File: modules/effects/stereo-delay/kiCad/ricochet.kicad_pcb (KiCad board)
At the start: 2 copper layers, 81 x 111 mm, 37 parts, among them J1 INPUT, J2 OUTPUT, J3 PWR, U1 TL074

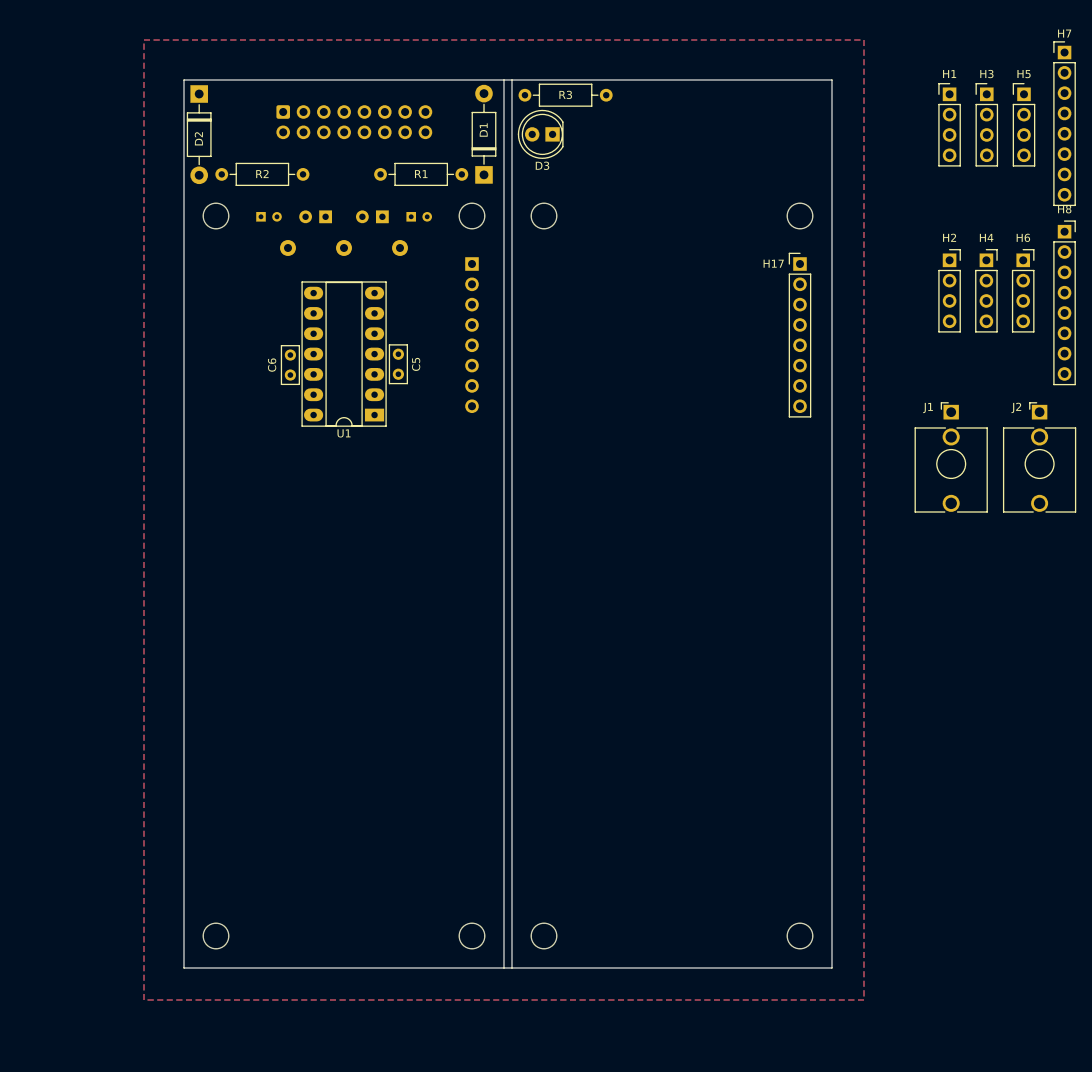
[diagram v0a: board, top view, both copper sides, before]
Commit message: Midi 2 CV (Midas) Rework; Delay (Richochet) Rework. Programming, backups for WeAct CV
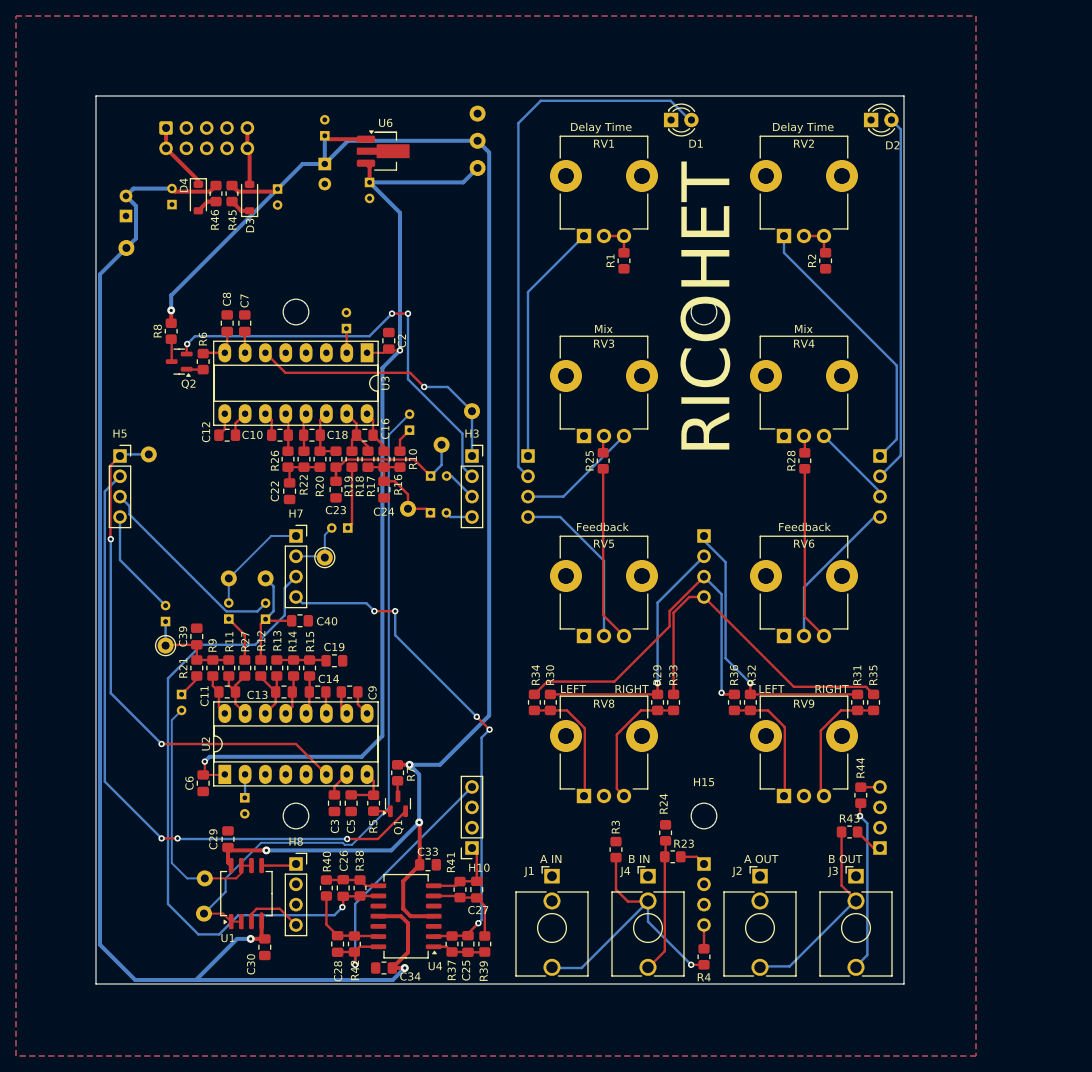
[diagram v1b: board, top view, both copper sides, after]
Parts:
- removed H16: MountingHole, MountingHole:MountingHole_3.2mm_M3
- removed H17: H17, Synth:PinHeader_1x08_P2.54mm_Vertical
- removed H18: H18, Synth:PinSocket_1x08_P2.54mm_Vertical
- added C10: 100nF, Capacitor_SMD:C_0805_2012Metric_Pad1.18x1.45mm_HandSolder, F.Cu at (73.0, 92.4)
- added C11: 560pF, Capacitor_SMD:C_0805_2012Metric_Pad1.18x1.45mm_HandSolder, F.Cu at (66.4, 124.5)
- added C12: 100nF, Capacitor_SMD:C_0805_2012Metric_Pad1.18x1.45mm_HandSolder, F.Cu at (66.4, 92.4)
- added C13: 560pF, Capacitor_SMD:C_0805_2012Metric_Pad1.18x1.45mm_HandSolder, F.Cu at (73.5, 124.5)
- added C14: 100nF, Capacitor_SMD:C_0805_2012Metric_Pad1.18x1.45mm_HandSolder, F.Cu at (77.7, 124.5)
- added C15: 4.7uF, Capacitor_THT:CP_Radial_D4.0mm_P2.00mm, B.Cu at (89.2, 91.8)
- added C16: 560pF, Capacitor_SMD:C_0805_2012Metric_Pad1.18x1.45mm_HandSolder, F.Cu at (83.6, 92.4)
- added C17: 4.7uF, Capacitor_THT:CP_Radial_D4.0mm_P2.00mm, B.Cu at (60.7, 124.8)
- added C18: 560pF, Capacitor_SMD:C_0805_2012Metric_Pad1.18x1.45mm_HandSolder, F.Cu at (77.0, 92.4)
- added C19: 3.3nF, Capacitor_SMD:C_0805_2012Metric_Pad1.18x1.45mm_HandSolder, F.Cu at (79.8, 120.6)
- added C20: 4.7uF, Capacitor_THT:CP_Radial_D4.0mm_P2.00mm, B.Cu at (58.7, 115.7)
- added C21: 10uF, Capacitor_THT:CP_Radial_D4.0mm_P2.00mm, B.Cu at (71.2, 115.4)
- added C22: 3.3nF, Capacitor_SMD:C_0805_2012Metric_Pad1.18x1.45mm_HandSolder, F.Cu at (74.2, 99.4)
- added C23: 10nF, Capacitor_SMD:C_0805_2012Metric_Pad1.18x1.45mm_HandSolder, F.Cu at (80.0, 99.2)
- added C24: 3.9nF, Capacitor_SMD:C_0805_2012Metric_Pad1.18x1.45mm_HandSolder, F.Cu at (86.0, 99.2)
- added C25: 27pF, Capacitor_SMD:C_0805_2012Metric_Pad1.18x1.45mm_HandSolder, F.Cu at (96.5, 156.0)
- added C26: 27pF, Capacitor_SMD:C_0805_2012Metric_Pad1.18x1.45mm_HandSolder, F.Cu at (80.9, 149.0)
- added C27: 47pF, Capacitor_SMD:C_0805_2012Metric_Pad1.18x1.45mm_HandSolder, F.Cu at (97.6, 149.2)
- added C28: 47pF, Capacitor_SMD:C_0805_2012Metric_Pad1.18x1.45mm_HandSolder, F.Cu at (80.2, 156.0)
- added C29: 0.1uF, Capacitor_SMD:C_0805_2012Metric_Pad1.18x1.45mm_HandSolder, F.Cu at (66.5, 142.9)
- added C30: 0.1uF, Capacitor_SMD:C_0805_2012Metric_Pad1.18x1.45mm_HandSolder, F.Cu at (71.1, 156.4)
- added C31: 47uF, Capacitor_THT:CP_Radial_D6.3mm_P2.50mm, B.Cu at (78.6, 58.5)
- added C32: 47uF, Capacitor_THT:CP_Radial_D6.3mm_P2.50mm, B.Cu at (53.8, 65.0)
- added C33: 0.1uF, Capacitor_SMD:C_0805_2012Metric_Pad1.18x1.45mm_HandSolder, F.Cu at (91.5, 146.1)
- added C34: 0.1uF, Capacitor_SMD:C_0805_2012Metric_Pad1.18x1.45mm_HandSolder, F.Cu at (86.0, 159.0)
- added C35: 0.1uF, Capacitor_THT:CP_Radial_D4.0mm_P2.00mm, B.Cu at (78.6, 55.0)
- added C36: 0.1uF, Capacitor_THT:CP_Radial_D4.0mm_P2.00mm, B.Cu at (59.5, 63.6)
- added C37: 0.1uF, Capacitor_THT:CP_Radial_D4.0mm_P2.00mm, B.Cu at (72.7, 61.6)
- added C38: 0.1uF, Capacitor_THT:CP_Radial_D4.0mm_P2.00mm, B.Cu at (84.2, 60.8)
- added C39: 3.9nF, Capacitor_SMD:C_0805_2012Metric_Pad1.18x1.45mm_HandSolder, F.Cu at (62.6, 117.6)
- added C40: 10nF, Capacitor_SMD:C_0805_2012Metric_Pad1.18x1.45mm_HandSolder, F.Cu at (75.5, 115.6)
- added C41: 10uF, Capacitor_THT:CP_Radial_D4.0mm_P2.00mm, B.Cu at (66.6, 115.4)
- added C42: 10uF, Capacitor_THT:CP_Radial_D4.0mm_P2.00mm, B.Cu at (81.5, 104.0)
- added C43: 10uF, Capacitor_THT:CP_Radial_D4.0mm_P2.00mm, B.Cu at (91.8, 97.5)
- added C44: 4.7uF, Capacitor_THT:CP_Radial_D4.0mm_P2.00mm, B.Cu at (91.8, 102.1)
- added C7: 100nF, Capacitor_SMD:C_0805_2012Metric_Pad1.18x1.45mm_HandSolder, F.Cu at (68.6, 78.4)
- added C8: 100nF, Capacitor_SMD:C_0805_2012Metric_Pad1.18x1.45mm_HandSolder, F.Cu at (66.4, 78.4)
- added C9: 100nF, Capacitor_SMD:C_0805_2012Metric_Pad1.18x1.45mm_HandSolder, F.Cu at (81.7, 124.5)
- added D4: 1N5819, Diode_SMD:D_SOD-123, F.Cu at (62.8, 62.7)
- added J4: INPUT, Synth:Jack_3.5mm_QingPu_WQP-PJ398SM_Vertical_CircularHoles, F.Cu at (119.0, 154.0)
- added Q1: 2N3904, Package_TO_SOT_SMD:SOT-23, F.Cu at (87.8, 138.5)
- added Q2: 2N3904, Package_TO_SOT_SMD:SOT-23, F.Cu at (60.4, 83.2)
- added R10: 15K, Resistor_SMD:R_0805_2012Metric_Pad1.20x1.40mm_HandSolder, F.Cu at (88.0, 95.4)
- added R11: 10K, Resistor_SMD:R_0805_2012Metric_Pad1.20x1.40mm_HandSolder, F.Cu at (66.6, 121.5)
- added R12: 5.6K, Resistor_SMD:R_0805_2012Metric_Pad1.20x1.40mm_HandSolder, F.Cu at (70.6, 121.5)
- added R13: 15K, Resistor_SMD:R_0805_2012Metric_Pad1.20x1.40mm_HandSolder, F.Cu at (72.6, 121.5)
- added R14: 10K, Resistor_SMD:R_0805_2012Metric_Pad1.20x1.40mm_HandSolder, F.Cu at (74.7, 121.5)
- added R15: 10K, Resistor_SMD:R_0805_2012Metric_Pad1.20x1.40mm_HandSolder, F.Cu at (76.7, 121.5)
- added R16: 10K, Resistor_SMD:R_0805_2012Metric_Pad1.20x1.40mm_HandSolder, F.Cu at (86.0, 95.4)
- added R17: 10K, Resistor_SMD:R_0805_2012Metric_Pad1.20x1.40mm_HandSolder, F.Cu at (84.0, 95.4)
- added R18: 4.7K, Resistor_SMD:R_0805_2012Metric_Pad1.20x1.40mm_HandSolder, F.Cu at (82.0, 95.4)
- added R19: 5.6K, Resistor_SMD:R_0805_2012Metric_Pad1.20x1.40mm_HandSolder, F.Cu at (80.0, 95.4)
- added R20: 15K, Resistor_SMD:R_0805_2012Metric_Pad1.20x1.40mm_HandSolder, F.Cu at (78.0, 95.4)
- added R21: 15K, Resistor_SMD:R_0805_2012Metric_Pad1.20x1.40mm_HandSolder, F.Cu at (62.6, 121.5)
- added R22: 10K, Resistor_SMD:R_0805_2012Metric_Pad1.20x1.40mm_HandSolder, F.Cu at (76.0, 95.4)
- added R23: 1K, Resistor_SMD:R_0805_2012Metric_Pad1.20x1.40mm_HandSolder, F.Cu at (122.1, 145.1)
- added R24: 100K, Resistor_SMD:R_0805_2012Metric_Pad1.20x1.40mm_HandSolder, F.Cu at (121.2, 142.1)
- added R25: 10K, Resistor_SMD:R_0805_2012Metric_Pad1.20x1.40mm_HandSolder, F.Cu at (113.4, 95.6)
- added R26: 10K, Resistor_SMD:R_0805_2012Metric_Pad1.20x1.40mm_HandSolder, F.Cu at (74.0, 95.4)
- added R27: 4.7K, Resistor_SMD:R_0805_2012Metric_Pad1.20x1.40mm_HandSolder, F.Cu at (68.6, 121.5)
- added R28: 10K, Resistor_SMD:R_0805_2012Metric_Pad1.20x1.40mm_HandSolder, F.Cu at (138.6, 95.6)
- added R29: 10K, Resistor_SMD:R_0805_2012Metric_Pad1.20x1.40mm_HandSolder, F.Cu at (120.2, 125.8)
- added R30: 10K, Resistor_SMD:R_0805_2012Metric_Pad1.20x1.40mm_HandSolder, F.Cu at (106.8, 125.8)
- added R31: 10K, Resistor_SMD:R_0805_2012Metric_Pad1.20x1.40mm_HandSolder, F.Cu at (145.2, 125.8)
- added R32: 10K, Resistor_SMD:R_0805_2012Metric_Pad1.20x1.40mm_HandSolder, F.Cu at (131.8, 125.8)
- added R33: 10K, Resistor_SMD:R_0805_2012Metric_Pad1.20x1.40mm_HandSolder, F.Cu at (122.2, 125.8)
- added R34: 10K, Resistor_SMD:R_0805_2012Metric_Pad1.20x1.40mm_HandSolder, F.Cu at (104.8, 125.8)
- added R35: 10K, Resistor_SMD:R_0805_2012Metric_Pad1.20x1.40mm_HandSolder, F.Cu at (147.2, 125.8)
- added R36: 10K, Resistor_SMD:R_0805_2012Metric_Pad1.20x1.40mm_HandSolder, F.Cu at (129.8, 125.8)
- added R37: 33K, Resistor_SMD:R_0805_2012Metric_Pad1.20x1.40mm_HandSolder, F.Cu at (94.5, 156.0)
- added R38: 33K, Resistor_SMD:R_0805_2012Metric_Pad1.20x1.40mm_HandSolder, F.Cu at (83.0, 149.0)
- added R39: 10K, Resistor_SMD:R_0805_2012Metric_Pad1.20x1.40mm_HandSolder, F.Cu at (98.6, 156.0)
- added R4: 1K, Resistor_SMD:R_0805_2012Metric_Pad1.20x1.40mm_HandSolder, F.Cu at (126.0, 157.6)
- added R40: 10K, Resistor_SMD:R_0805_2012Metric_Pad1.20x1.40mm_HandSolder, F.Cu at (78.8, 149.0)
- added R41: 10K, Resistor_SMD:R_0805_2012Metric_Pad1.20x1.40mm_HandSolder, F.Cu at (95.5, 149.2)
- added R42: 10K, Resistor_SMD:R_0805_2012Metric_Pad1.20x1.40mm_HandSolder, F.Cu at (82.3, 156.0)
- added R43: 1K, Resistor_SMD:R_0805_2012Metric_Pad1.20x1.40mm_HandSolder, F.Cu at (144.2, 142.0)
- added R44: 1K, Resistor_SMD:R_0805_2012Metric_Pad1.20x1.40mm_HandSolder, F.Cu at (145.6, 137.4)
- added R45: 10R, Resistor_SMD:R_0805_2012Metric_Pad1.20x1.40mm_HandSolder, F.Cu at (67.0, 62.2)
- added R46: 10R, Resistor_SMD:R_0805_2012Metric_Pad1.20x1.40mm_HandSolder, F.Cu at (65.0, 62.2)
- added R5: 1K, Resistor_SMD:R_0805_2012Metric_Pad1.20x1.40mm_HandSolder, F.Cu at (84.7, 138.4)
- added R6: 1K, Resistor_SMD:R_0805_2012Metric_Pad1.20x1.40mm_HandSolder, F.Cu at (63.4, 83.2)
- added R7: 100K, Resistor_SMD:R_0805_2012Metric_Pad1.20x1.40mm_HandSolder, F.Cu at (87.7, 134.6)
- added R8: 100K, Resistor_SMD:R_0805_2012Metric_Pad1.20x1.40mm_HandSolder, F.Cu at (59.4, 79.4)
- added R9: 10K, Resistor_SMD:R_0805_2012Metric_Pad1.20x1.40mm_HandSolder, F.Cu at (64.6, 121.5)
- added RV1: B50K, Synth:Potentiometer_TT_P0915N, F.Cu at (113.5, 60.0)
- added RV2: B50K, Synth:Potentiometer_TT_P0915N, F.Cu at (138.5, 60.0)
- added RV3: B100K, Synth:Potentiometer_TT_P0915N, F.Cu at (113.5, 85.0)
- added RV4: B100K, Synth:Potentiometer_TT_P0915N, F.Cu at (138.5, 85.0)
- added RV5: B100K, Synth:Potentiometer_TT_P0915N, F.Cu at (113.5, 110.0)
- added RV6: B100K, Synth:Potentiometer_TT_P0915N, F.Cu at (138.5, 110.0)
- added RV8: B25K, Synth:Potentiometer_TT_P0915N, F.Cu at (113.5, 130.0)
- added RV9: B25K, Synth:Potentiometer_TT_P0915N, F.Cu at (138.5, 130.0)
- added TP10: POST_FEEDBACK_CH_2, Connector_Pin:Pin_D1.0mm_L10.0mm, F.Cu at (58.7, 118.7)
- added TP11: POST_FEEDBACK_CH_1, Connector_Pin:Pin_D1.0mm_L10.0mm, B.Cu at (89.0, 101.6)
- added TP12: MIX_INPUT_CH_2, Connector_Pin:Pin_D1.0mm_L10.0mm, B.Cu at (71.2, 110.3)
- added TP13: MIX_INPUT_CH_1, Connector_Pin:Pin_D1.0mm_L10.0mm, B.Cu at (93.2, 93.6)
- added TP14: +5V, Connector_Pin:Pin_D1.0mm_L10.0mm, B.Cu at (97.7, 59.0)
- added TP4: INPUT_CH_1, Connector_Pin:Pin_D1.0mm_L10.0mm, B.Cu at (63.5, 152.2)
- added TP5: INPUT_CH_2, Connector_Pin:Pin_D1.0mm_L10.0mm, B.Cu at (63.6, 147.8)
- added TP6: OUTPUT_CH_1, Connector_Pin:Pin_D1.0mm_L10.0mm, F.Cu at (78.6, 107.7)
- added TP7: OUTPUT_CH_2, Connector_Pin:Pin_D1.0mm_L10.0mm, B.Cu at (66.6, 110.3)
- added TP8: DELAY_TIME_CH_2, Connector_Pin:Pin_D1.0mm_L10.0mm, B.Cu at (56.6, 94.8)
- added TP9: DELAY_TIME_CH_1, Connector_Pin:Pin_D1.0mm_L10.0mm, B.Cu at (97.0, 89.4)
- added U2: PT2399, Package_DIP:DIP-16_W7.62mm_Socket_LongPads, F.Cu at (66.1, 134.8)
- added U3: PT2399, Package_DIP:DIP-16_W7.62mm_Socket_LongPads, F.Cu at (83.9, 82.1)
- added U4: TL074, Package_SO:SO-14_5.3x10.2mm_P1.27mm, F.Cu at (88.8, 152.5)
- added U6: L7805, Package_TO_SOT_SMD:SOT-89-3_Handsoldering, F.Cu at (86.2, 56.9)
- C1: value 47uF -> 10uF; footprint Capacitor_THT:CP_Radial_D6.3mm_P2.50mm -> Capacitor_THT:CP_Radial_D4.0mm_P2.00mm
- C2: value 47uF -> 100nF; footprint Capacitor_THT:CP_Radial_D6.3mm_P2.50mm -> Capacitor_SMD:C_0805_2012Metric_Pad1.18x1.45mm_HandSolder; moved to F.Cu
- C3: value 0.1uF -> 100nF; footprint Capacitor_THT:CP_Radial_D4.0mm_P2.00mm -> Capacitor_SMD:C_0805_2012Metric_Pad1.18x1.45mm_HandSolder; moved to F.Cu
- C4: value 0.1uF -> 10uF
- C5, C6: value 0.1uF -> 100nF; footprint Capacitor_THT:C_Rect_L4.6mm_W2.0mm_P2.50mm_MKS02_FKP02 -> Capacitor_SMD:C_0805_2012Metric_Pad1.18x1.45mm_HandSolder
- D1, D2: value 1N5819 -> LED; footprint Synth:D_DO-41_SOD81_P10.16mm_Horizontal -> Synth:LED_D3.0mm
- D3: value LED -> 1N5819; footprint Synth:LED_D5.0mm (center Aligned) -> Diode_SMD:D_SOD-123
- H1: value H1 -> Conn_02x05_PWR_Eurorack; footprint Synth:PinHeader_1x04_P2.54mm_Vertical -> Synth:IDC-Header_2x05_P2.54mm_Vertical; moved to B.Cu
- H10: value MountingHole -> PinSocket_01x04; footprint MountingHole:MountingHole_3.2mm_M3 -> Synth:PinSocket_1x04_P2.54mm_Vertical
- H11, H9: value MountingHole -> PinHeader_01x04; footprint MountingHole:MountingHole_3.2mm_M3 -> Synth:PinHeader_1x04_P2.54mm_Vertical; moved to B.Cu
- H2: value H3 -> PinHeader_01x04; footprint Synth:PinSocket_1x04_P2.54mm_Vertical -> Synth:PinHeader_1x04_P2.54mm_Vertical; moved to B.Cu
- H3: value H5 -> PinSocket_01x04; footprint Synth:PinHeader_1x04_P2.54mm_Vertical -> Synth:PinSocket_1x04_P2.54mm_Vertical
- H4: value H6 -> PinHeader_01x04; footprint Synth:PinSocket_1x04_P2.54mm_Vertical -> Synth:PinHeader_1x04_P2.54mm_Vertical; moved to B.Cu
- H5: value H7 -> PinSocket_01x04; footprint Synth:PinHeader_1x04_P2.54mm_Vertical -> Synth:PinSocket_1x04_P2.54mm_Vertical
- H6: value H8 -> PinHeader_01x04; footprint Synth:PinSocket_1x04_P2.54mm_Vertical -> Synth:PinHeader_1x04_P2.54mm_Vertical; moved to B.Cu
- H7: value H2 -> PinSocket_01x04; footprint Synth:PinHeader_1x08_P2.54mm_Vertical -> Synth:PinSocket_1x04_P2.54mm_Vertical
- H8: value H4 -> PinSocket_01x04; footprint Synth:PinSocket_1x08_P2.54mm_Vertical -> Synth:PinSocket_1x04_P2.54mm_Vertical
- J2: value OUTPUT -> L/MONO_OUTPUT
- J3: value PWR -> R_OUTPUT; footprint Synth:IDC-Header_2x08_P2.54mm_Vertical -> Synth:Jack_3.5mm_QingPu_WQP-PJ398SM_Vertical_CircularHoles; moved to F.Cu
- R1, R2: value 10 -> 2K; footprint Synth:R_Default (DIN0207) -> Resistor_SMD:R_0805_2012Metric_Pad1.20x1.40mm_HandSolder
- R3: value 500R -> 100K; footprint Synth:R_Default (DIN0207) -> Resistor_SMD:R_0805_2012Metric_Pad1.20x1.40mm_HandSolder
- U1: value TL074 -> TL072; footprint Package_DIP:DIP-14_W7.62mm_Socket_LongPads -> Package_SO:SO-8_5.3x6.2mm_P1.27mm
- moved J3 124.6 mm to (145.0, 154.0), turned to 0 degrees
- moved H8 124.4 mm to (75.0, 146.0)
- moved H5 121.7 mm to (53.0, 95.0)
- moved H7 113.5 mm to (75.0, 105.0)
- moved H13 100.3 mm to (75.0, 77.0)
- moved H1 98.0 mm to (58.8, 54.0), turned to -90 degrees
- moved R3 95.0 mm to (115.0, 144.2), turned to -90 degrees
- moved H11 89.5 mm to (148.0, 144.0)
- moved D2 85.4 mm to (148.2, 53.0), turned to 0 degrees
- moved H9 81.9 mm to (126.0, 146.0), turned to 180 degrees
- moved H10 79.0 mm to (97.0, 144.0), turned to 180 degrees
- moved H3 78.6 mm to (97.0, 95.0)
- moved J1 76.5 mm to (107.0, 154.0)
- moved R2 76.2 mm to (141.2, 70.6), turned to 90 degrees
- moved C1 74.6 mm to (68.6, 137.7), turned to -90 degrees
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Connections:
- net Net-(U1A--) renamed /PT2399_delay-module_channel_1/delay_input
- net Net-(U1B--) renamed /PT2399_delay-module_channel_2/delay_input
- C1 pad 1: +12V -> Net-(U2-REF)
- C2 pad 2: -12V -> +5V
- C3 pad 1: +12V -> Net-(U2-CC1)
- C4 pad 1: GNDREF -> Net-(U3-REF)
- C4 pad 2: -12V -> GNDREF
- C5 pad 1: +12V -> Net-(U2-CC0)
- C6 pad 2: -12V -> +5V
- D1 pad 1: Net-(D1-K) -> GNDREF
- D2 pad 1: Net-(D2-K) -> GNDREF
- D3 pad 2: +12V -> Net-(D3-A)
- H1 pad 1: unconnected-(H1A-Pin_1-Pad1) -> Net-(D4-K)
- H1 pad 2: unconnected-(H1B-Pin_2-Pad2) -> Net-(D4-K)
- H1 pad 3: unconnected-(H1C-Pin_3-Pad3) -> GNDREF
- H1 pad 4: unconnected-(H1D-Pin_4-Pad4) -> GNDREF
- H2 pad 1: unconnected-(H2A-Pin_1-Pad1) -> Net-(H2A-Pin_1)
- H2 pad 2: unconnected-(H2B-Pin_2-Pad2) -> Net-(D2-A)
- H2 pad 3: unconnected-(H2C-Pin_3-Pad3) -> Net-(H2C-Pin_3)
- H2 pad 4: unconnected-(H2D-Pin_4-Pad4) -> Net-(H2D-Pin_4)
- H3 pad 1: unconnected-(H3A-Pin_1-Pad1) -> Net-(H3A-Pin_1)
- H3 pad 2: unconnected-(H3B-Pin_2-Pad2) -> Net-(H3B-Pin_2)
- H3 pad 3: unconnected-(H3C-Pin_3-Pad3) -> Net-(H3C-Pin_3)
- H3 pad 4: unconnected-(H3D-Pin_4-Pad4) -> Net-(H3D-Pin_4)
- H4 pad 1: unconnected-(H4A-Pin_1-Pad1) -> Net-(H4A-Pin_1)
- H4 pad 2: unconnected-(H4B-Pin_2-Pad2) -> Net-(D1-A)
- H4 pad 3: unconnected-(H4C-Pin_3-Pad3) -> Net-(H4C-Pin_3)
- H4 pad 4: unconnected-(H4D-Pin_4-Pad4) -> Net-(H4D-Pin_4)
- H5 pad 1: unconnected-(H5A-Pin_1-Pad1) -> Net-(H5A-Pin_1)
- H5 pad 2: unconnected-(H5B-Pin_2-Pad2) -> Net-(H5B-Pin_2)
- H5 pad 3: unconnected-(H5C-Pin_3-Pad3) -> Net-(H5C-Pin_3)
- H5 pad 4: unconnected-(H5D-Pin_4-Pad4) -> Net-(H5D-Pin_4)
- H6 pad 1: unconnected-(H6A-Pin_1-Pad1) -> Net-(H6A-Pin_1)
- H6 pad 2: unconnected-(H6B-Pin_2-Pad2) -> Net-(H6B-Pin_2)
- H6 pad 3: unconnected-(H6C-Pin_3-Pad3) -> Net-(H6C-Pin_3)
- H6 pad 4: unconnected-(H6D-Pin_4-Pad4) -> Net-(H6D-Pin_4)
- H7 pad 1: unconnected-(H7A-Pin_1-Pad1) -> /PT2399_delay-module_channel_2/delay_output
- H7 pad 2: unconnected-(H7B-Pin_2-Pad2) -> /PT2399_delay-module_channel_1/delay_output
- H7 pad 3: unconnected-(H7C-Pin_3-Pad3) -> Net-(H7C-Pin_3)
- H7 pad 4: unconnected-(H7D-Pin_4-Pad4) -> Net-(H7D-Pin_4)
- H8 pad 1: unconnected-(H8A-Pin_3-Pad1) -> Net-(H8A-Pin_1)
- H8 pad 2: unconnected-(H8B-Pin_2-Pad2) -> GNDREF
- H8 pad 3: unconnected-(H8C-Pin_3-Pad3) -> GNDREF
- H8 pad 4: unconnected-(H8D-Pin_4-Pad4) -> Net-(H8D-Pin_4)
- J1 pad T: unconnected-(J1-PadT) -> Net-(J1-PadT)
- J1 pad TN: unconnected-(J1-PadTN) -> GNDREF
- J2 pad T: unconnected-(J2-PadT) -> Net-(J2-PadT)
- R1 pad 1: Net-(D1-K) -> GNDREF
- R1 pad 2: +12V -> Net-(R1-Pad2)
- R2 pad 1: Net-(D2-A) -> GNDREF
- R2 pad 2: -12V -> Net-(R2-Pad2)
- R3 pad 2: Net-(D3-K) -> Net-(J1-PadT)
- U1 pad 3: GNDREF -> Net-(H8D-Pin_4)
- U1 pad 4: +12V -> -12V
- U1 pad 5: GNDREF -> Net-(H8A-Pin_1)
- U1 pad 8: Net-(U1C--) -> +12V
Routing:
- net +12V: track 0.00 -> 202.7 mm, vias 0 -> 4
- net -12V: track 0.00 -> 174.7 mm, vias 0 -> 2
- net +5V: track 0.00 -> 121.5 mm, vias 0 -> 2
- net /PT2399_delay-module_channel_1/delay_input: track 0.00 -> 85.2 mm
- net Net-(H7C-Pin_3): track 0.00 -> 82.1 mm, vias 0 -> 1
- net Net-(H5B-Pin_2): track 0.00 -> 81.0 mm, vias 0 -> 3
- net Net-(D1-A): track 0.00 -> 68.4 mm
- net Net-(H5A-Pin_1): track 0.00 -> 65.0 mm, vias 0 -> 2
- net Net-(H7D-Pin_4): track 0.00 -> 64.0 mm, vias 0 -> 5
- net Net-(H3B-Pin_2): track 0.00 -> 54.1 mm, vias 0 -> 3
- net Net-(D2-A): track 0.00 -> 46.1 mm
- net Net-(H6C-Pin_3): track 0.00 -> 45.5 mm, vias 0 -> 1
- net Net-(H6D-Pin_4): track 0.00 -> 41.1 mm
- net Net-(J1-PadT): track 0.00 -> 35.8 mm, vias 0 -> 1
- net Net-(H6A-Pin_1): track 0.00 -> 35.6 mm, vias 0 -> 1
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- added copper zone on F.Cu, net GNDREF
- removed copper zone on F.Cu, net (none)
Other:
- board size 81 x 111 mm -> 101 x 111 mm
- board text added: "+5V"
- board text added: "A IN"
- board text added: "A OUT"
- board text added: "B IN"
- board text added: "B OUT"
- board text added: "Delay Time"
- board text added: "Feedback"
- board text added: "LEFT"
- board text added: "Mix"
- board text added: "RICOHET"
- board text added: "RIGHT"

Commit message: finish up PCB finals for run-2, continue on C code for midas/sequencer
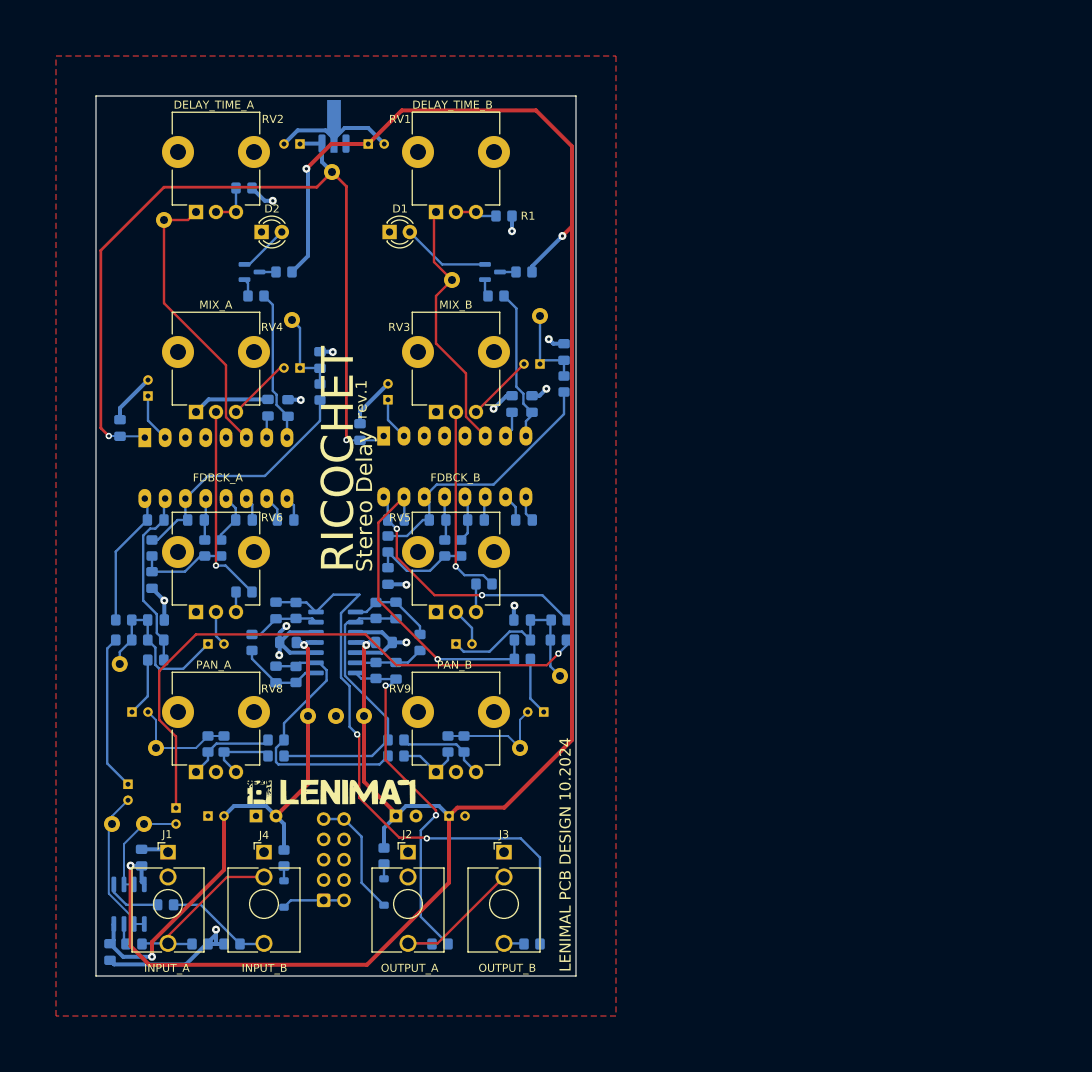
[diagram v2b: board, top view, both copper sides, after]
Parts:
- removed H10, H3, H5, H7, H8: PinSocket_01x04, Synth:PinSocket_1x04_P2.54mm_Vertical
- removed H11, H2, H4, H6, H9: PinHeader_01x04, Synth:PinHeader_1x04_P2.54mm_Vertical
- removed H12, H13, H14, H15: MountingHole, MountingHole:MountingHole_3.2mm_M3
- added G***: LOGO, Synth:lenimal_logo_full, F.Cu at (79.5, 137.0)
- C10, C11, C12, C13, C14, C16, C18, C19, C2, C22, C23, C24, C25, C26, C27, C28, C3, C39, C40, C5, C6, C7, C8, C9, D3, D4, Q1, Q2, R1, R10, R11, R12, R13, R14, R15, R16, R17, R18, R19, R2, R20, R21, R22, R23, R24, R25, R26, R27, R28, R29, R3, R30, R31, R32, R33, R34, R35, R36, R37, R38, R39, R4, R40, R41, R42, R43, R44, R45, R46, R5, R6, R9, TP10, TP6, U2, U3, U6: moved to B.Cu
- C29, C30, C33, C34: value 0.1uF -> 100nF; moved to B.Cu
- C35, C36, C37, C38: value 0.1uF -> 100nF
- J2: value L/MONO_OUTPUT -> OUTPUT
- J3: value R_OUTPUT -> OUTPUT
- R7, R8: value 100K -> 680R; moved to B.Cu
- RV8, RV9: value B25K -> B10K
- U1: footprint Package_SO:SO-8_5.3x6.2mm_P1.27mm -> Synth:SOIC-8; moved to B.Cu
- U4: footprint Package_SO:SO-14_5.3x10.2mm_P1.27mm -> Synth:SOIC-14; moved to B.Cu
- moved H1 98.5 mm to (78.5, 150.5), turned to 0 degrees
- moved D3 88.4 mm to (86.0, 149.5), turned to -90 degrees
- moved D4 87.7 mm to (73.5, 149.8), turned to 90 degrees
- moved C35 86.4 mm to (94.1, 140.0), turned to 0 degrees
- moved R45 85.0 mm to (86.0, 145.0)
- moved R46 83.5 mm to (73.5, 145.2)
- moved C31 82.0 mm to (87.5, 140.0), turned to 0 degrees
- moved D2 77.5 mm to (72.0, 67.0)
- moved TP2 77.4 mm to (80.0, 127.5)
- moved C32 76.7 mm to (70.0, 140.0), turned to 0 degrees
- moved C36 76.6 mm to (64.0, 140.0), turned to 0 degrees
- moved RV2 73.6 mm to (65.0, 57.0)
- moved RV4 73.6 mm to (65.0, 82.0)
- moved RV6 73.6 mm to (65.0, 107.0)
- moved TP1 73.3 mm to (83.5, 127.5), turned to 180 degrees
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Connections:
- C20 pad 2: Net-(H5D-Pin_4) -> Net-(C20-Pad2)
- C21 pad 2: Net-(H5C-Pin_3) -> Net-(C21-Pad2)
- C25 pad 1: Net-(H7D-Pin_4) -> Net-(U4A--)
- C26 pad 1: Net-(H7C-Pin_3) -> Net-(U4C--)
- C27 pad 2: Net-(H10A-Pin_1) -> Net-(C27-Pad2)
- C28 pad 2: Net-(H10D-Pin_4) -> Net-(C28-Pad2)
- C43 pad 2: Net-(H3C-Pin_3) -> Net-(C43-Pad2)
- C44 pad 2: Net-(H3D-Pin_4) -> Net-(C44-Pad2)
- C6 pad 1: GNDREF -> +5V
- C6 pad 2: +5V -> GNDREF
- Q1 pad 2: Net-(H5B-Pin_2) -> Net-(D1-A)
- Q2 pad 2: Net-(H3B-Pin_2) -> Net-(D2-A)
- R23 pad 1: Net-(H9A-Pin_1) -> Net-(U1B-+)
- R29 pad 1: Net-(H6B-Pin_2) -> /PT2399_delay-module_channel_1/delay_output
- R30 pad 1: Net-(H6B-Pin_2) -> /PT2399_delay-module_channel_1/delay_output
- R31 pad 1: Net-(H6A-Pin_1) -> /PT2399_delay-module_channel_2/delay_output
- R32 pad 1: Net-(H6A-Pin_1) -> /PT2399_delay-module_channel_2/delay_output
- R33 pad 2: Net-(H6D-Pin_4) -> Net-(U4A--)
- R34 pad 2: Net-(H6C-Pin_3) -> Net-(U4C--)
- R35 pad 2: Net-(H6D-Pin_4) -> Net-(U4A--)
- R36 pad 2: Net-(H6C-Pin_3) -> Net-(U4C--)
- R37 pad 1: Net-(H7D-Pin_4) -> Net-(U4A--)
- R38 pad 1: Net-(H7C-Pin_3) -> Net-(U4C--)
- R4 pad 1: Net-(H9D-Pin_4) -> Net-(U1A-+)
- R41 pad 2: Net-(H10A-Pin_1) -> Net-(C27-Pad2)
- R42 pad 2: Net-(H10D-Pin_4) -> Net-(C28-Pad2)
- R43 pad 2: Net-(H11A-Pin_1) -> Net-(C27-Pad2)
- R44 pad 2: Net-(H11D-Pin_4) -> Net-(C28-Pad2)
- RV1 pad 1: Net-(H4A-Pin_1) -> Net-(U2-VCO)
- RV2 pad 1: Net-(H2A-Pin_1) -> Net-(U3-VCO)
- RV3 pad 3: Net-(H4C-Pin_3) -> Net-(C21-Pad2)
- RV4 pad 3: Net-(H2C-Pin_3) -> Net-(C43-Pad2)
- RV5 pad 2: Net-(H4D-Pin_4) -> Net-(C20-Pad2)
- RV6 pad 2: Net-(H2D-Pin_4) -> Net-(C44-Pad2)
- TP8 pad 1: Net-(H5A-Pin_1) -> Net-(U2-VCO)
- TP9 pad 1: Net-(H3A-Pin_1) -> Net-(U3-VCO)
- U1 pad 3: Net-(H8D-Pin_4) -> Net-(U1A-+)
- U1 pad 5: Net-(H8A-Pin_1) -> Net-(U1B-+)
- U2 pad 6: Net-(H5A-Pin_1) -> Net-(U2-VCO)
- U3 pad 6: Net-(H3A-Pin_1) -> Net-(U3-VCO)
- U4 pad 14: Net-(H10D-Pin_4) -> Net-(C28-Pad2)
- U4 pad 2: Net-(H7D-Pin_4) -> Net-(U4A--)
- U4 pad 7: Net-(H10A-Pin_1) -> Net-(C27-Pad2)
- U4 pad 9: Net-(H7C-Pin_3) -> Net-(U4C--)
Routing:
- net GNDREF: track 0.00 -> 111.5 mm, vias 0 -> 14
- net -12V: track 174.7 -> 68.1 mm
- net Net-(H7C-Pin_3): track 82.1 -> 0.00 mm, vias 1 -> 0
- net Net-(H5B-Pin_2): track 81.0 -> 0.00 mm, vias 3 -> 0
- net Net-(C28-Pad2): track 0.00 -> 75.6 mm, vias 0 -> 2
- net Net-(C17-Pad1): track 3.09 -> 74.1 mm, vias 0 -> 1
- net /PT2399_delay-module_channel_1/delay_input: track 85.2 -> 19.0 mm
- net Net-(H5A-Pin_1): track 65.0 -> 0.00 mm, vias 2 -> 0
- net Net-(H7D-Pin_4): track 64.0 -> 0.00 mm, vias 5 -> 0
- net +12V: track 202.7 -> 261.5 mm
- net Net-(D1-A): track 68.4 -> 11.1 mm
- net Net-(H3B-Pin_2): track 54.1 -> 0.00 mm, vias 3 -> 0
- net Net-(H6C-Pin_3): track 45.5 -> 0.00 mm, vias 1 -> 0
- net Net-(C27-Pad2): track 0.00 -> 44.1 mm, vias 0 -> 2
- net Net-(H6D-Pin_4): track 41.1 -> 0.00 mm
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- removed copper zone on B.Cu, net (none)
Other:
- board size 101 x 111 mm -> 60 x 110 mm
- board text added: "DELAY_TIME"
- board text added: "DELAY_TIME_A"
- board text added: "DELAY_TIME_B"
- board text added: "DLY_IN"
- board text added: "DLY_OUT"
- board text added: "FDBCK"
- board text added: "FDBCK_A"
- board text added: "FDBCK_B"
- board text added: "INPUT_A"
- board text added: "INPUT_B"
- board text added: "L7805"
- board text added: "LENIMAL PCB DESIGN 10.2024"
- board text added: "MIX"
- board text added: "MIX_A"
- board text added: "MIX_B"
- board text added: "OUTPUT_A"
- board text added: "OUTPUT_B"
- board text added: "PAN_A"
- board text added: "PAN_B"
- board text added: "PT2399"
- board text added: "RICOCHET"
- board text added: "Stereo Delay"
- board text added: "TL072"
- board text added: "TL074"
- board text added: "rev.1"
- board text removed: "+12V"
- board text removed: "-12V"
- board text removed: "A IN"
- board text removed: "A OUT"
- board text removed: "B IN"
- board text removed: "B OUT"
- board text removed: "Delay Time"
- board text removed: "Feedback"
- board text removed: "GND"
- board text removed: "LEFT"
- board text removed: "Mix"
- board text removed: "RICOHET"
- board text removed: "RIGHT"
